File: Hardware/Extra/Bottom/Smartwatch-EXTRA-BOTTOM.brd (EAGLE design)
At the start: 33 x 33 mm, 37 parts, among them U1 AD5242-SO16, U3 PCF8523

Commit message: Extra features updated
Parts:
- removed C19: 2.2n, LinnesLab-Passives:C0603
- removed C20: 22u, LinnesLab-Passives:C0603
- removed R23: 1M, LinnesLab-Passives:R0603
- removed R24: 10k, LinnesLab-Passives:R0603
- removed XTAL2: 32.7680kHz, LinnesLab-Clocks:2-SMD.NOLEAD.2.0MMTO1.2MM
- added C3, C4: 100n, LinnesLab-Passives:C0603
- added J2: (no value), LinnesLab-Connectors:1X02_1.27MM
- added R1, R2: 10k, LinnesLab-Passives:R0603
- added XTAL1: 32.7680kHz, LinnesLab-Clocks:2-SMD.NOLEAD.2.0MMTO1.2MM
- C10: value 100n -> 2.2n
- C11: value 100n -> 22u
- J1: device LinnesLab-Connectors:1X07 -> LinnesLab-Connectors:1X07_1.27MM
- R13: value 220k -> 1M
- R14: value 10M -> 10k
- R3: value 10k -> 220k
- R4: value 10k -> 10M
- moved R3 24.9 mm to (33.4, 5.81), turned to 270 degrees
- moved R13 21.5 mm to (28.9, 26.8), turned to 180 degrees
- moved R4 19.2 mm to (27.6, 10.7)
- moved U3 17.7 mm to (11.8, 23.9), turned to 90 degrees
- moved C10 14.1 mm to (28.9, 24.7)
- moved R14 5.02 mm to (23.3, 8.01), turned to 270 degrees
- moved C11 3.40 mm to (21.0, 7.94), turned to 270 degrees
- renumbered C14 to C5, C15 to C6, C16 to C7, C17 to C8, C18 to C9, C21 to C12, C22 to C13, R15 to R5, R16 to R6, R17 to R7, R18 to R8, R19 to R9, R20 to R10, R21 to R11, R22 to R12, U$3 to U2, U$4 to U4
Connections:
- net 3.3V: now also C4.2, R1.2, R2.2; no longer C11.2, R13.2, R4.2
- net A6/TIA: now also C3.2; no longer C10.2
- net G.W2: now also R14.1; no longer R24.1
- net GND: now also C4.1; no longer C11.1
- net N$13: now also R3.1; no longer R13.1
- net N$15: now also R4.1; no longer R14.1
- net N$16: now also R4.2; no longer R14.2
- net N$18: now also C10.2, R13.2; no longer C19.2, R23.2
- net N$19: now also C10.1, C11.1; no longer C19.1, C20.1
- net N$2: now also XTAL1.P$1; no longer XTAL2.P$1
- net N$20: now also C11.2, R14.2; no longer C20.2, R24.2
- net N$3: now also XTAL1.P$2; no longer XTAL2.P$2
- net PD.C: now also C3.1; no longer C10.1
- net SCL: now also R1.1; no longer R3.1
- net SDA: now also R2.1; no longer R4.1
- net VREF: now also R13.1; no longer R23.1
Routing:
- net SDA: track 75.0 -> 49.6 mm, vias 4 -> 5
- net SCL: track 57.5 -> 37.5 mm, vias 3 -> 2
- net D26/LED.CTRL: track 22.7 -> 16.5 mm
- net N$19: track 23.5 -> 20.3 mm
- net A6/TIA: track 55.0 -> 54.4 mm, vias 2 -> 1
- net N$17: track 10.4 -> 10.9 mm

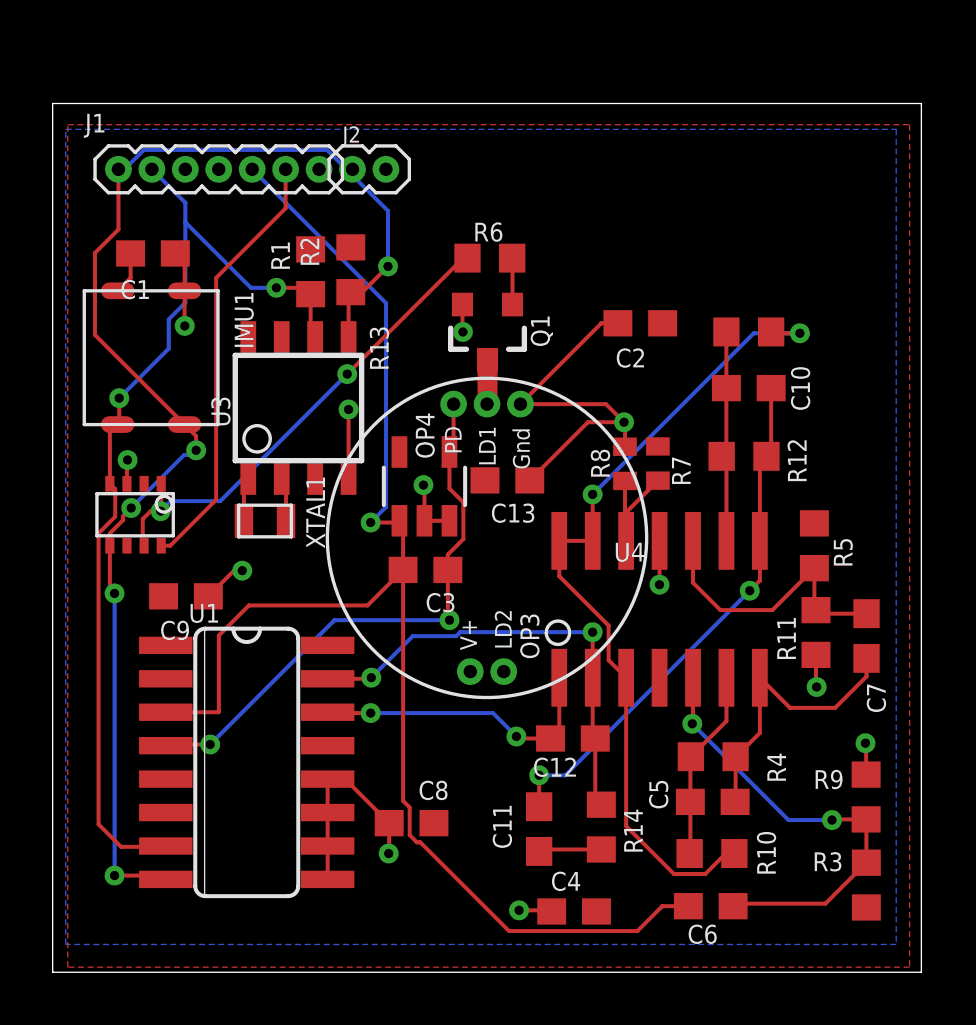
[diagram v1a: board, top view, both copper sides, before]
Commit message: Extra Silkscreens updated
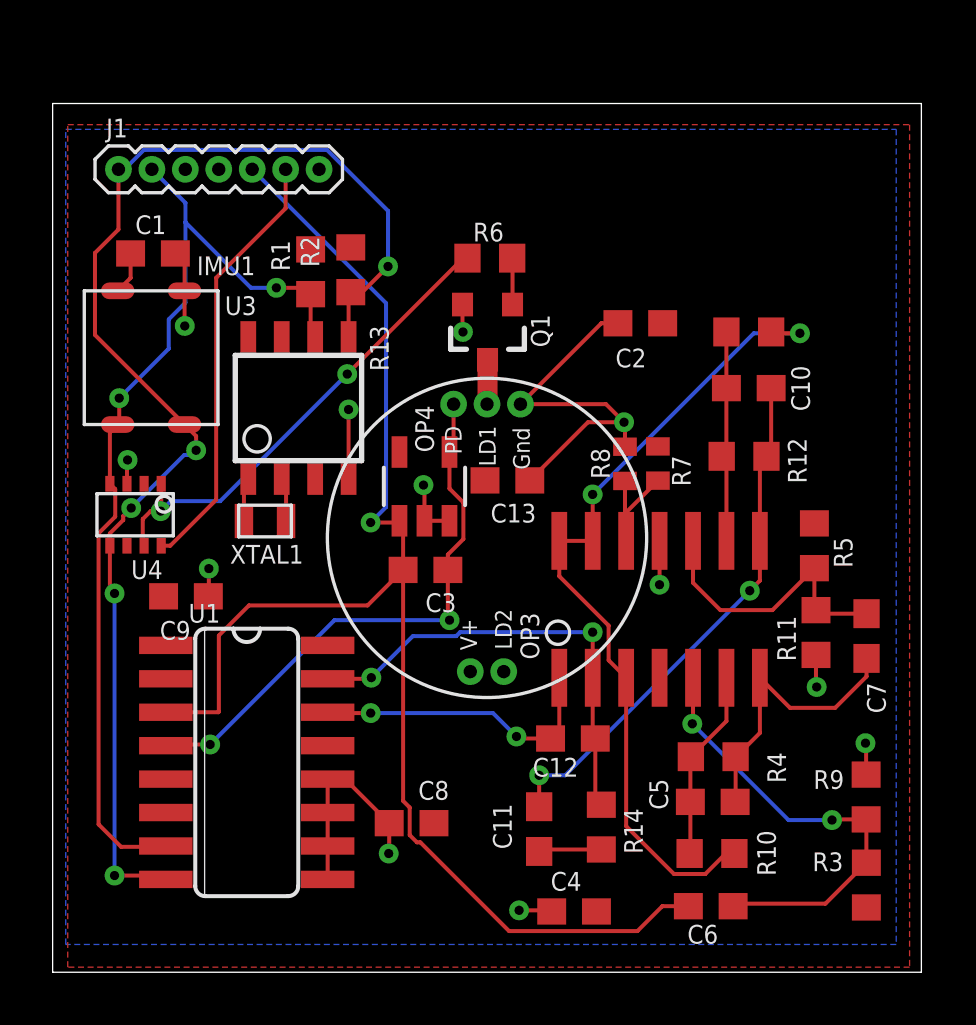
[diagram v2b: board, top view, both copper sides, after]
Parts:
- removed J2: (no value), LinnesLab-Connectors:1X02_1.27MM
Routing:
- net GND: track 39.5 -> 38.9 mm
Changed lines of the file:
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@@
 </element>
 <element name="U4" library="LinnesLab-DigitalIC" package="SOT-23-8" package3d_urn="urn:adsk.eagle:package:17879439/2" value="AD5171" x="5.6332" y="19.8788" smashed="yes" rot="R180" grouprefs="PPG">
-<attribute name="NAME" x="25.0162" y="18.8138" size="0.7112" layer="25" rot="R180"/>
+<attribute name="NAME" x="6.679940625" y="18.1508625" size="0.7112" layer="25" rot="R180"/>
 <attribute name="VALUE" x="8.5332" y="22.8788" size="0.6604" layer="27" rot="R180"/>
 </element>
@@
 </element>
 <element name="OP4" library="LinnesLab-AnalogIC" package="SOT23-5" value="" x="16.624" y="20.955" smashed="yes" grouprefs="PPG">
-<attribute name="NAME" x="16.2944" y="23.7744" size="0.7112" layer="25" ratio="10" rot="R270"/>
+<attribute name="NAME" x="16.27408125" y="24.0284" size="0.7112" layer="25" ratio="10" rot="R270"/>
 <attribute name="VALUE" x="19.672" y="19.177" size="1.27" layer="27" ratio="10" rot="R90"/>
 </element>
@@
 <attribute name="FREQ" value="32.7680KHZ" x="10.592" y="20.555" size="1.778" layer="27" rot="R180" display="off"/>
 <attribute name="LOAD_CAP" value="12.5pF" x="10.592" y="20.555" size="1.778" layer="27" rot="R180" display="off"/>
-<attribute name="NAME" x="12.8454" y="18.589" size="0.7112" layer="25" rot="R90"/>
+<attribute name="NAME" x="12.02561875" y="18.733121875" size="0.7112" layer="25" rot="R180"/>
 <attribute name="VALUE" x="12.3228" y="22.2502" size="0.7112" layer="27" rot="R180"/>
 </element>
@@
 <attribute name="MFN" value="PCF8523T/1,118" x="11.8366" y="23.9332" size="1.778" layer="27" rot="R90" display="off"/>
 <attribute name="MFN_MANUFACTURER" value="NXP USA Inc." x="11.8366" y="23.9332" size="1.778" layer="27" rot="R90" display="off"/>
-<attribute name="NAME" x="9.2458" y="23.1966" size="0.7112" layer="25" rot="R90"/>
+<attribute name="NAME" x="10.2425" y="28.17641875" size="0.7112" layer="25" rot="R180"/>
 <attribute name="VALUE" x="15.3926" y="22.0282" size="0.7112" layer="27" rot="R90"/>
 </element>
 <element name="J1" library="LinnesLab-Connectors" package="1X07_1.27MM" value="" x="5" y="33" smashed="yes">
-<attribute name="NAME" x="3.73" y="34.397" size="0.7112" layer="25" font="vector" ratio="20"/>
+<attribute name="NAME" x="4.532640625" y="34.214121875" size="0.7112" layer="25" font="vector" ratio="20"/>
 <attribute name="VALUE" x="3.73" y="30.968" size="0.6096" layer="27" font="vector" ratio="20"/>
 </element>
 <element name="IMU1" library="LinnesLab-Sensors" package="LSM6DS3_CAST" value="LSM6DS3_CAST" x="6.2418" y="25.8448" smashed="yes" rot="R270">
-<attribute name="NAME" x="9.4168" y="28.3848" size="0.7112" layer="25" rot="R270"/>
+<attribute name="NAME" x="7.977840625" y="28.97988125" size="0.7112" layer="25"/>
 <attribute name="VALUE" x="1.7968" y="28.3848" size="0.6604" layer="27" rot="R270"/>
 </element>
 <element name="C1" library="LinnesLab-Passives" package="C0603" package3d_urn="urn:adsk.eagle:package:15661989/2" value="100n" x="6.3114" y="29.8034" smashed="yes" rot="R180">
-<attribute name="NAME" x="6.2352" y="28.7874" size="0.7112" layer="25" rot="R180"/>
+<attribute name="NAME" x="6.8092375" y="31.2512" size="0.7112" layer="25" rot="R180"/>
 <attribute name="VALUE" x="6.9464" y="31.7084" size="0.6604" layer="27" rot="R180"/>
-</element>
-<element name="J2" library="LinnesLab-Connectors" package="1X02_1.27MM" value="" x="13.89" y="33" smashed="yes">
-<attribute name="NAME" x="13.509" y="34.016" size="0.6096" layer="25" font="vector" ratio="20"/>
-<attribute name="VALUE" x="13.509" y="31.349" size="0.6096" layer="27" font="vector" ratio="20"/>
 </element>
 </elements>
@@
 <wire x1="20.6242" y1="21.1836" x2="22.834" y2="23.3934" width="0.1524" layer="1"/>
 <wire x1="22.834" y1="23.3934" x2="24.2062" y2="23.3934" width="0.1524" layer="1"/>
-<wire x1="8.4136" y1="16.78" x2="9.3882" y2="17.7546" width="0.1524" layer="1"/>
-<wire x1="9.3882" y1="17.7546" x2="9.7028" y2="17.7546" width="0.1524" layer="1"/>
-<via x="9.7028" y="17.7546" extent="1-16" drill="0.35"/>
+<wire x1="8.4136" y1="16.78" x2="8.4328" y2="16.7992" width="0.1524" layer="1"/>
+<wire x1="8.4328" y1="16.7992" x2="8.4328" y2="17.833340625" width="0.1524" layer="1"/>
+<via x="8.4328" y="17.833340625" extent="1-16" drill="0.35"/>
 </signal>
 <signal name="3.3V">

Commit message: Encoder Added, Silkscreen Updated, Bom Updated
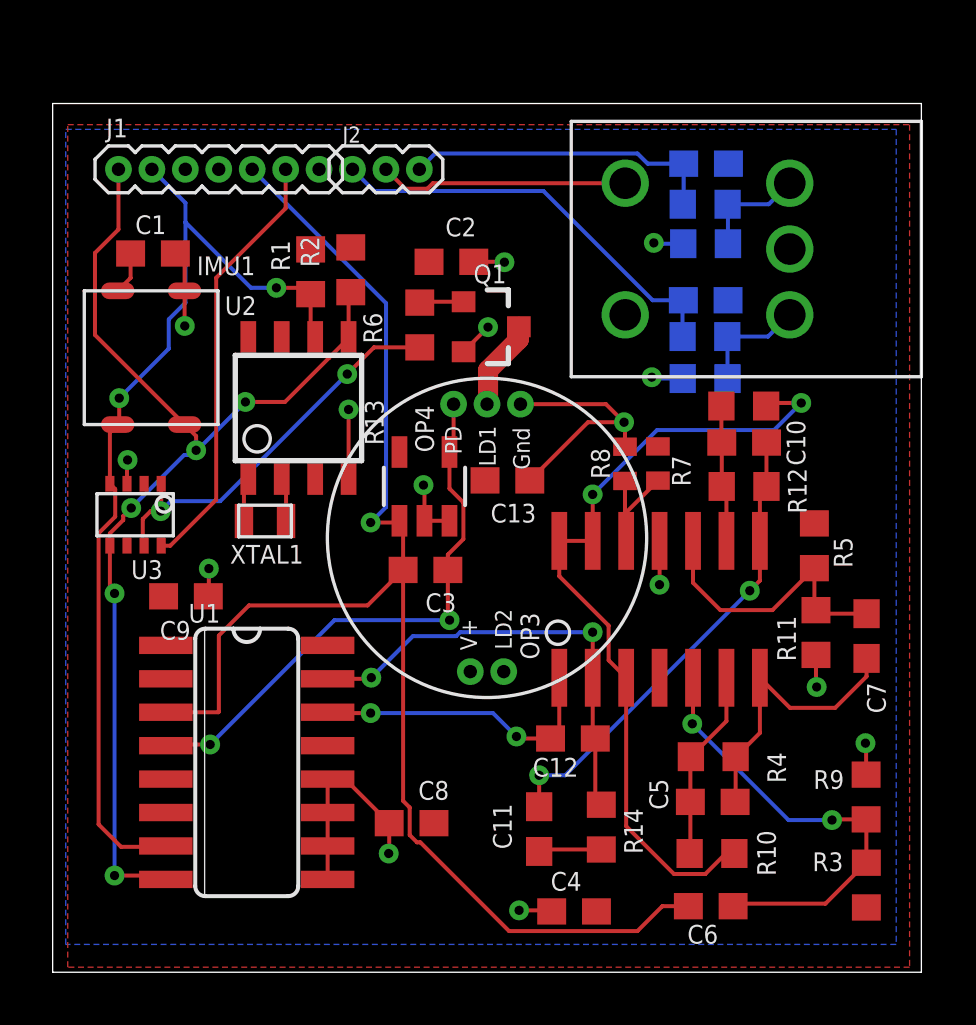
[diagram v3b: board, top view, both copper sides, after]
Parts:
- added C14, C15: 10 nF, LinnesLab-Passives:C0603
- added ENC1: PEC09-2220F-S0012, Encoder:ENCODER
- added J2: (no value), LinnesLab-Connectors:1X03_1.27MM
- added R15, R16, R17, R18: 10k, LinnesLab-Passives:R0603
- U2: value (none) -> PCF8523; device LinnesLab-Connectors:PPG.MODULE.2 -> LinnesLab-Clocks:SO8
- U3: value PCF8523 -> AD5171; device LinnesLab-Clocks:SO8 -> LinnesLab-DigitalIC:SOT-23-8
- U4: value AD5171 -> (none); device LinnesLab-DigitalIC:SOT-23-8 -> LinnesLab-Connectors:PPG.MODULE.2
- moved U4 13.4 mm to (19.0, 19.0), turned to 0 degrees
- moved U2 8.70 mm to (11.8, 23.9), turned to 90 degrees
- moved C2 7.55 mm to (17.6, 29.5), turned to 0 degrees
- moved U3 7.41 mm to (5.63, 19.9), turned to 180 degrees
- moved R6 3.68 mm to (16.4, 27.1), turned to 90 degrees
- moved R13 2.82 mm to (28.8, 24.0)
- moved C10 2.07 mm to (28.8, 22.6)
- moved R12 1.15 mm to (28.8, 21.0)
- moved Q1 0.18 mm to (19.1, 27.0), turned to 270 degrees
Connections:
- new net A.OUT: C15.1, J2.1, R18.1
- new net B.OUT: C14.1, J2.3, R17.1
- new net MOM.BUTTON: ENC1.MOM.BUTTON, J2.2
- new net N$1: ENC1.A, R16.2, R18.2
- new net N$4: ENC1.B, R15.2, R17.2
- net 3.3V: now also ENC1.3.3V, R15.1, R16.1, U2.8, U3.2, U3.6, U4.V+; no longer U2.V+, U3.8, U4.2, U4.6
- net D26/LED.CTRL: now also U3.8; no longer U4.8
- net GND: now also C14.2, C15.2, ENC1.GND, U2.4, U3.3, U4.GND; no longer U2.GND, U3.4, U4.3
- net LED.C: now also U4.LD1; no longer U2.LD1
- net N$2: now also U2.2; no longer U3.2
- net N$3: now also U2.1; no longer U3.1
- net N$9: now also U3.1, U3.7; no longer U4.1, U4.7
- net PD.C: now also U4.PD; no longer U2.PD
- net SCL: now also U2.6, U3.4; no longer U3.6, U4.4
- net SDA: now also U2.5; no longer U4.5
- net VBATT: now also U2.3; no longer U3.3
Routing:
- net A.OUT: track 0.00 -> 16.0 mm
- net B.OUT: track 0.00 -> 12.0 mm
- net MOM.BUTTON: track 0.00 -> 9.48 mm
- net SDA: track 49.6 -> 41.7 mm
- net N$1: track 0.00 -> 4.31 mm
- net N$4: track 0.00 -> 4.20 mm
- net GND: track 38.9 -> 35.3 mm, vias 12 -> 13
- net N$9: track 18.5 -> 15.3 mm
- net N$18: track 8.08 -> 5.20 mm
- net 3.3V: track 1.62 -> 3.95 mm, vias 0 -> 2
- net N$19: track 20.3 -> 18.0 mm
- net LED.C: track 1.69 -> 3.44 mm
- net VREF: track 31.6 -> 30.9 mm

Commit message: Encoder changed, BOMs updated
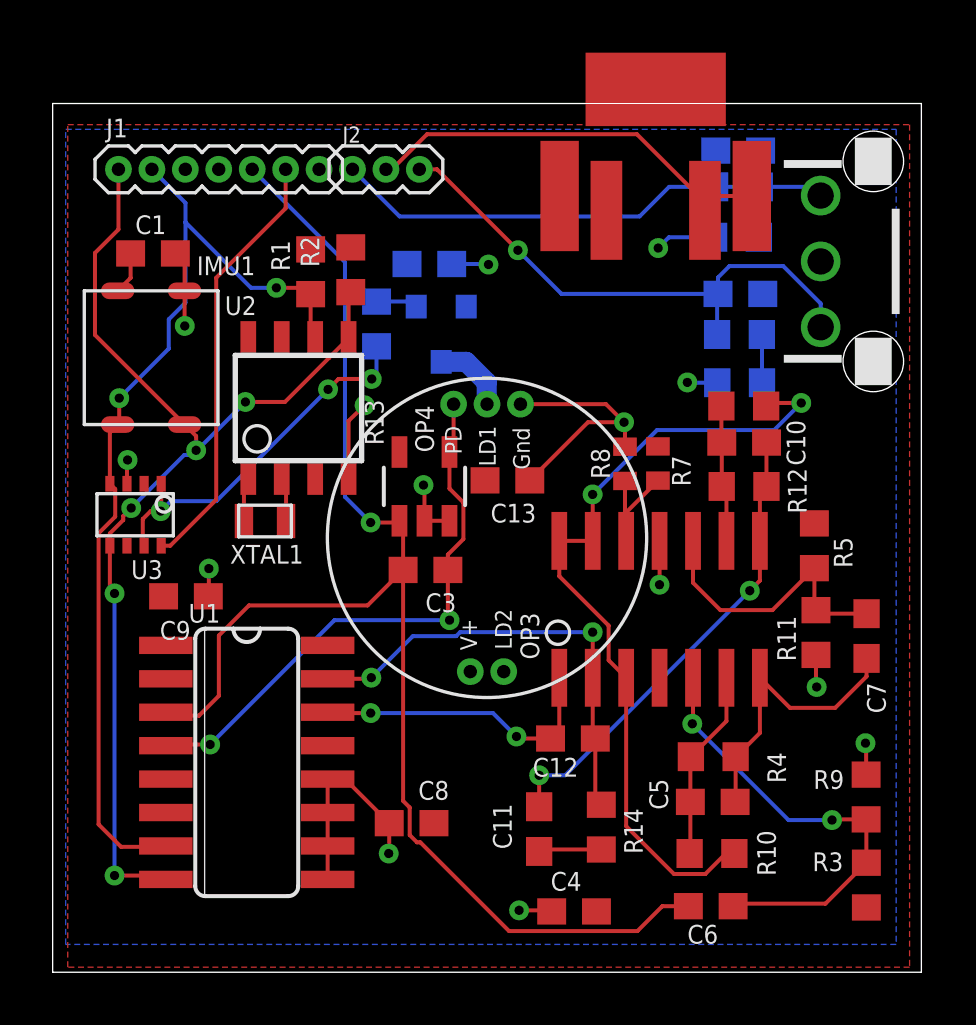
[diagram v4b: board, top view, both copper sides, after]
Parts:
- added B1: SWITCH, Encoder:SWITCH
- ENC1: value PEC09-2220F-S0012 -> EVQVU; device Encoder:ENCODER -> Encoder:EVQVU
- moved C15 5.82 mm to (28.5, 33.7)
- moved R18 5.82 mm to (28.5, 32.3)
- moved R16 5.50 mm to (28.5, 30.4)
- moved R15 5.44 mm to (28.6, 24.9)
- moved C14 5.12 mm to (28.6, 28.3)
- moved R17 5.12 mm to (28.6, 26.7)
- moved Q1 1.87 mm to (17.3, 26.8), flipped to the bottom, turned to 180 degrees
- moved R6 1.64 mm to (14.8, 27.1), flipped to the bottom
- moved ENC1 1.26 mm to (31.7, 29.5), turned to 90 degrees
- moved C2 0.84 mm to (16.8, 29.4), flipped to the bottom
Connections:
- removed net N$1: ENC1.A, R16.2, R18.2
- net 3.3V: now also B1.P$4, B1.P$5; no longer ENC1.3.3V
- net A.OUT: now also ENC1.P$2, R16.2, R18.2
- net B.OUT: now also ENC1.P$3
- net GND: now also ENC1.P$1; no longer ENC1.GND
- net MOM.BUTTON: now also B1.P$2, B1.P$3; no longer ENC1.MOM.BUTTON
- net N$4: no longer ENC1.B
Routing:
- net B.OUT: track 12.0 -> 21.0 mm, vias 0 -> 1
- net MOM.BUTTON: track 9.48 -> 16.1 mm
- net A.OUT: track 16.0 -> 22.5 mm
- net N$1: track 4.31 -> 0.00 mm
- net 3.3V: track 3.95 -> 6.46 mm, vias 2 -> 3
- net N$4: track 4.20 -> 1.83 mm
- net GND: track 35.3 -> 33.2 mm, vias 13 -> 11
- net N$9: track 15.3 -> 14.3 mm, vias 2 -> 3
- net A6/TIA: track 54.4 -> 53.7 mm
- net LED.C: track 3.44 -> 2.88 mm

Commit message: GPS Removed, added back original display, kept pads for adafruit display
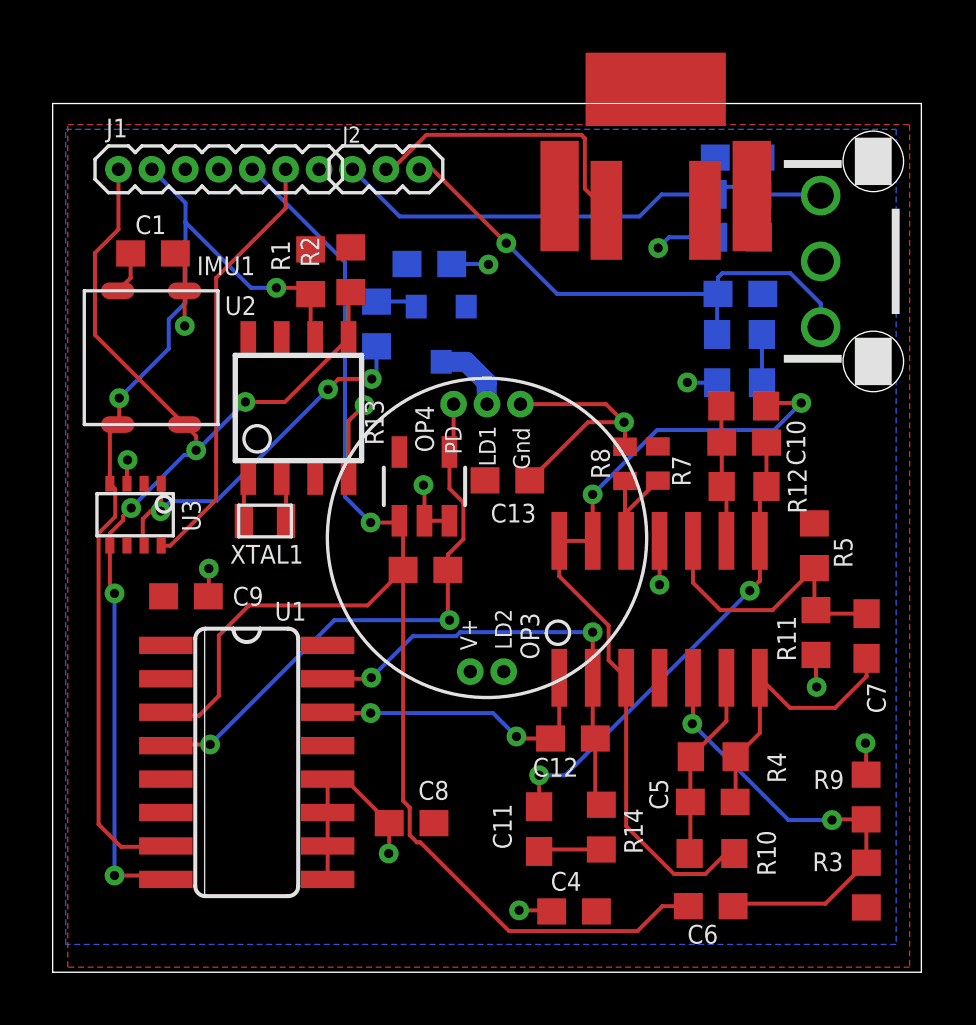
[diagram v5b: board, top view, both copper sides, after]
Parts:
- moved R18 0.29 mm to (28.5, 32.0)
- moved C15 0.27 mm to (28.5, 33.4)
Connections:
- net 3.3V: now also B1.P$3; no longer B1.P$4, B1.P$5
- net MOM.BUTTON: now also B1.P$4; no longer B1.P$2, B1.P$3
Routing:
- net MOM.BUTTON: track 16.1 -> 11.2 mm
